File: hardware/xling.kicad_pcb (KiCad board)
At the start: 2 copper layers, 35.6 x 48.3 mm, 58 parts, among them J4 USB_OTG, J5 AVR ISP, J6 Battery, Q1 NTR0202PL, Q2 NTR0202PL, Q3 NTA4153N, SW2 BTN, SW3 BTN, SW4 BTN, U1 LT1109CZ-12, U2 ATMEGA328P-AU, U3 DEP_128064I, U4 MCP73831, U5 AP3401_TSOT26, Y1 8MHz

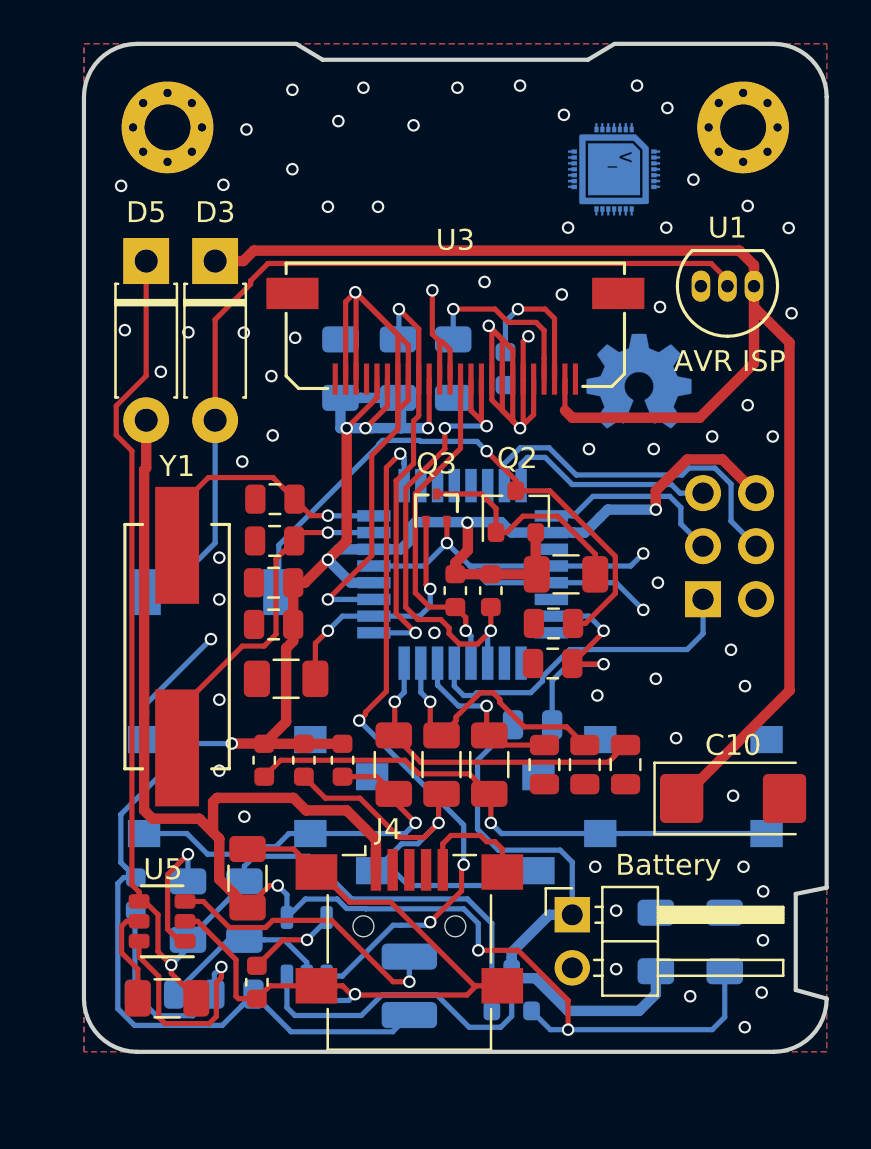
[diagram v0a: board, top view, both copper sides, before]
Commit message: patch 0.2.0004: Updated footprints.
Several footprints were updated to replaced rectangle pads with
rounded-corner pads. Minor PCB changes were made also.

Bill of materials can be found in the hardware directory.

Signed-off-by: Dmitry Salychev <darkness.bsd@gmail.com>
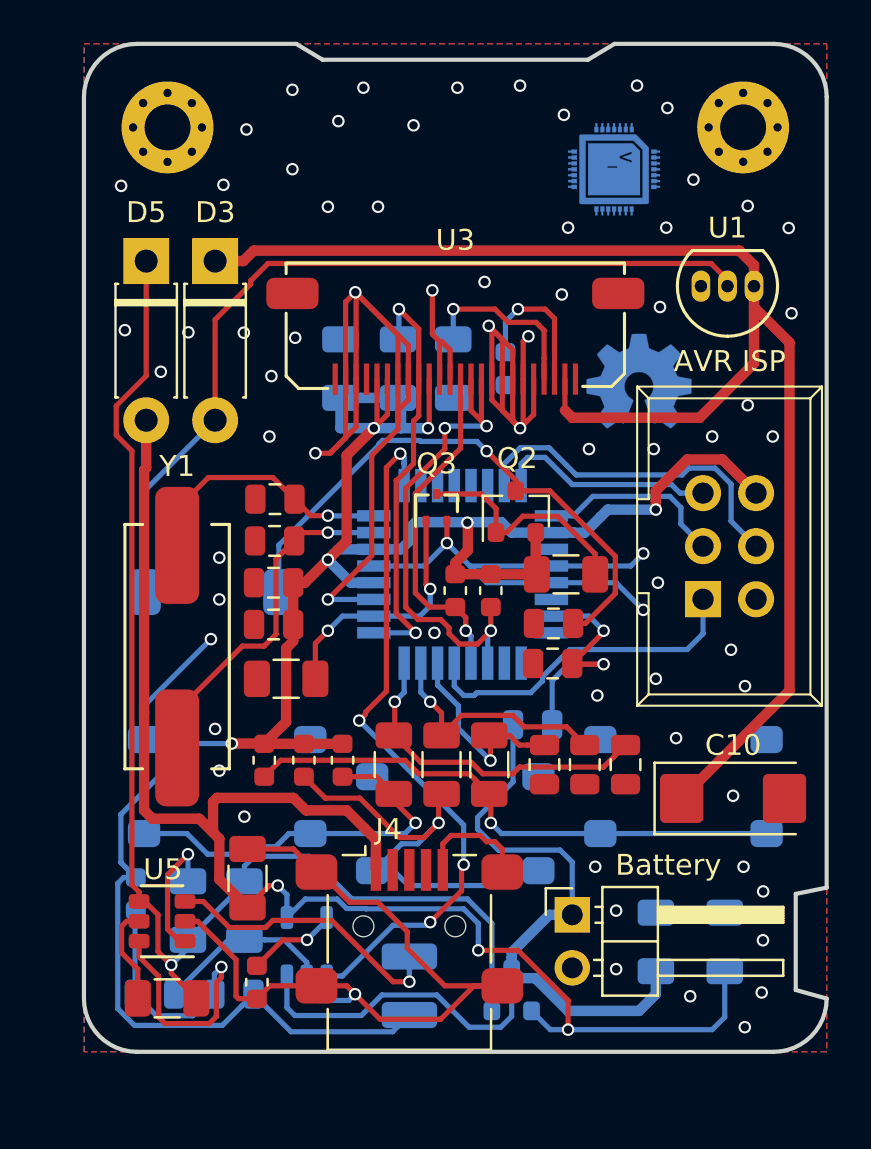
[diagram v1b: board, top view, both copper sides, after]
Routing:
- net GND: track 146.5 -> 157.8 mm
- net /BTN1: track 8.11 -> 10.6 mm
- net /BTN2: track 13.3 -> 12.2 mm
- net Net-(D3-Pad2): track 41.4 -> 40.8 mm
- net +3V3: track 109.3 -> 109.1 mm, vias 7 -> 6
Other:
- board text added: "Xling 0.2.0004 MCUSim.org"
- board text removed: "Xling 0.2.0003 MCUSim.org"

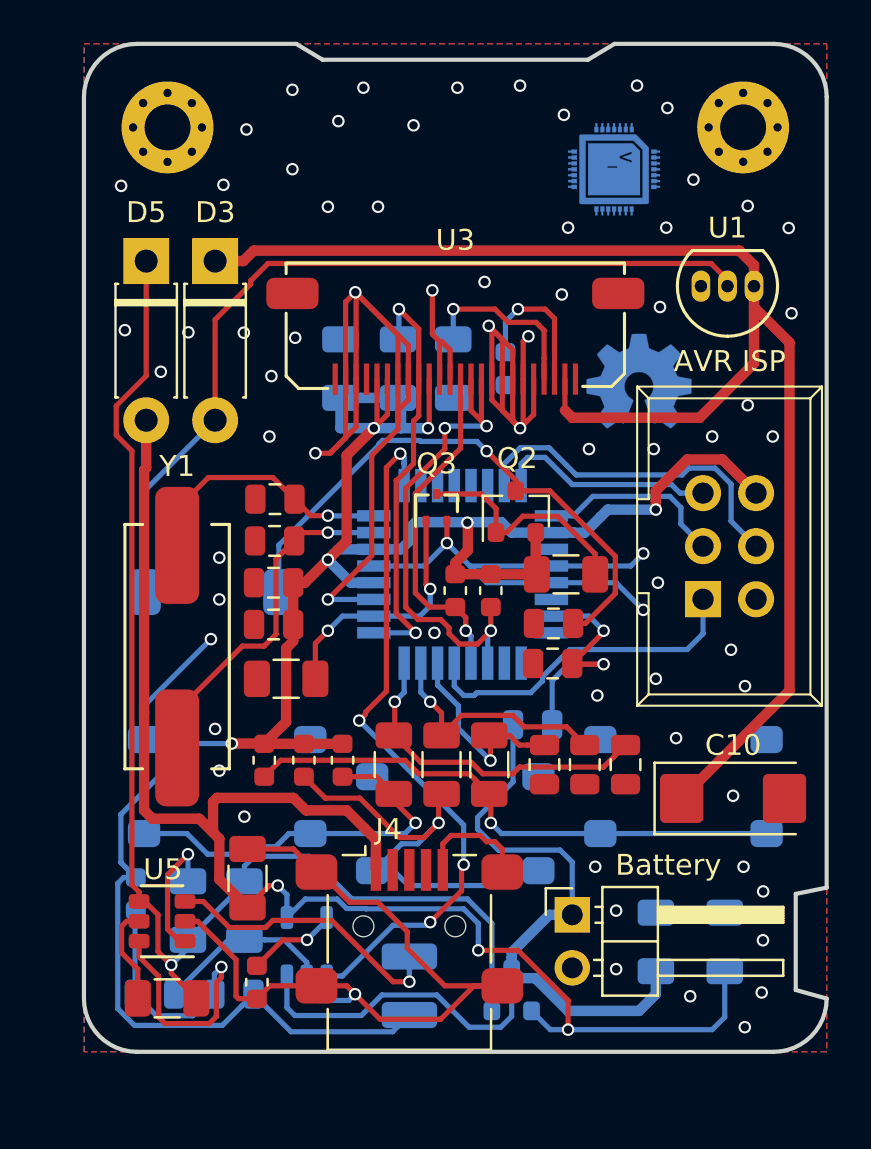
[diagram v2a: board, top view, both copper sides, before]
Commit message: patch 0.2.7: PCB adjustments.
ticket: N/A

There are some modifications to make a new version of the PCB ready for
manufacturing.
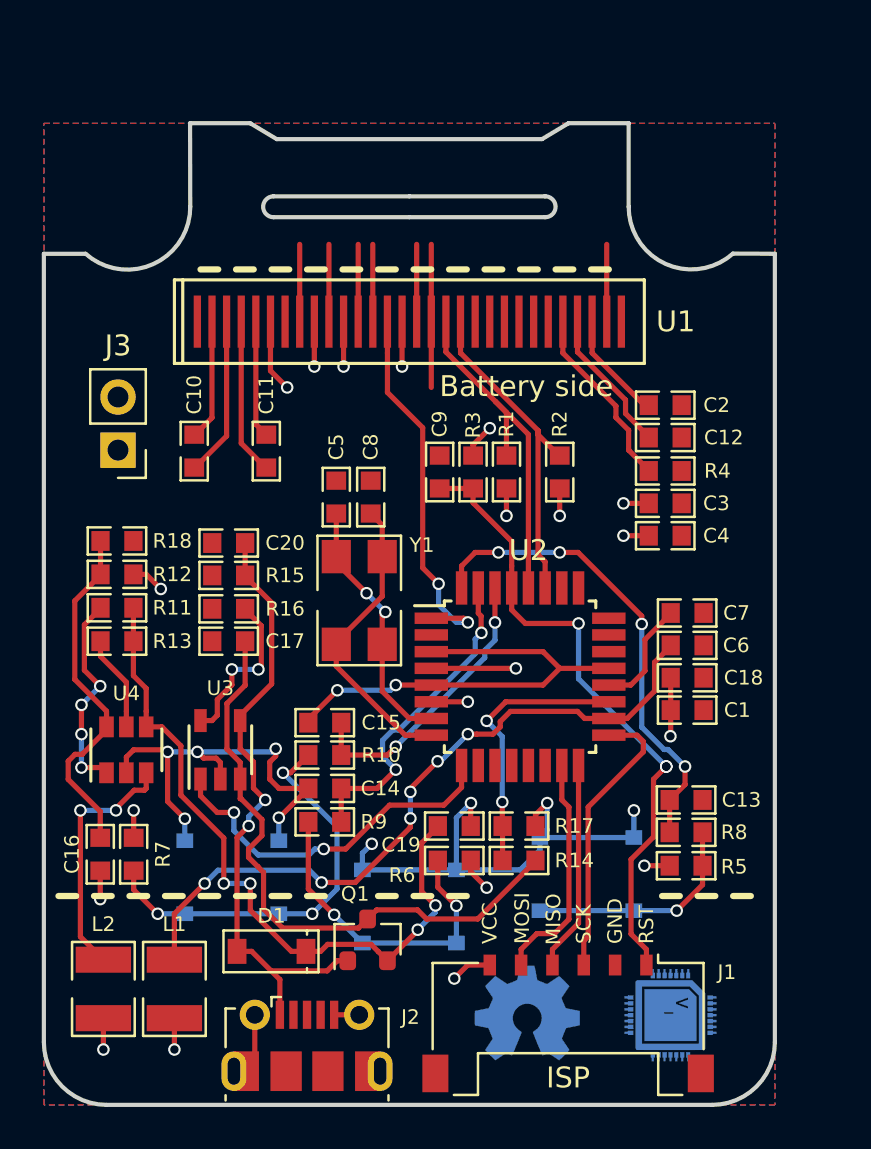
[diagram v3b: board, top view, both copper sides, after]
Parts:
- removed D3, D5: 1N5818, Xling Footprints:D_DO-41_SOD81_P7.62mm_Horizontal
- removed J4: USB_OTG, Xling Footprints:USB_Mini-B_Lumberg_2486_01_Horizontal
- removed J5: AVR ISP, Xling Footprints:IDC-Header_2x03_P2.54mm_Vertical
- removed J6: Battery, Xling Footprints:PinHeader_1x02_P2.54mm_Horizontal
- removed Q2: NTR0202PL, Xling Footprints:SOT-23
- removed Q3: NTA4153N, Xling Footprints:SC-75_SOT-416
- removed R19: 100K, Xling Footprints:R_1206_3216Metric
- removed R20: 110K, Xling Footprints:R_0805_2012Metric
- removed REF** (x2): MountingHole_2.2mm_M2_Pad_Via, MountingHole:MountingHole_2.2mm_M2_Pad_Via
- removed SW4: BTN, Xling Footprints:SW_SPST_PTS645
- removed U5: AP3401_TSOT26, Xling Footprints:AP3401_TSOT26
- added C12: 4.7uF, Xling Footprints:C_0603_1608Metric, F.Cu at (149.8, 95.0)
- added C14: 4.7nF, Xling Footprints:C_0603_1608Metric, F.Cu at (133.4, 111.8)
- added C16: 22pF, Xling Footprints:C_0603_1608Metric, F.Cu at (122.7, 115.0)
- added C17: 4.7uF, Xling Footprints:C_0603_1608Metric, F.Cu at (128.8, 104.8)
- added C4: 4.7uF, Xling Footprints:C_0603_1608Metric, F.Cu at (149.8, 99.8)
- added D1: 1N5819, Xling Footprints:D_SOD-123, F.Cu at (130.9, 119.7)
- added J1: ISP, Xling Footprints:Molex_Pico-Lock_504050-0691_1x06-1MP_P1.50mm_Horizontal, F.Cu at (145.1, 123.1)
- added J2: USB_OTG, Xling Footprints:USB_Micro-B_Molex-105017-0001, F.Cu at (132.6, 124.2)
- added J3: Battery, Xling Footprints:PinHeader_1x02_P2.54mm_Vertical, F.Cu at (123.5, 95.7)
- added SW1: BTN, Xling Footprints:SW_Tact_4.5x4.5mm_TVCM09BB_Low_Profile, B.Cu at (146.0, 116.0)
- C1: value 22pF -> 4.7nF; footprint Xling Footprints:C_0805_2012Metric -> Xling Footprints:C_0603_1608Metric; moved to F.Cu
- C10: value 33uF -> 0.22uF; footprint Xling Footprints:CP_EIA-6032-20_AVX-F -> Xling Footprints:C_0603_1608Metric
- C11: value 2.2uF -> 0.22uF; moved to F.Cu
- C13, C15: value 22pF -> 4.7nF; footprint Xling Footprints:C_0805_2012Metric -> Xling Footprints:C_0603_1608Metric
- C18, C19, C20: value 4.7nF -> 4.7uF; footprint Xling Footprints:C_0805_2012Metric -> Xling Footprints:C_0603_1608Metric
- C2: footprint Xling Footprints:C_1206_3216Metric -> Xling Footprints:C_0603_1608Metric; moved to F.Cu
- C3: footprint Xling Footprints:C_1206_3216Metric -> Xling Footprints:C_0603_1608Metric
- C5: value 4.7uF -> 22pF; footprint Xling Footprints:C_1206_3216Metric -> Xling Footprints:C_0603_1608Metric; moved to F.Cu
- C6: value 4.7uF -> 100nF; footprint Xling Footprints:C_1206_3216Metric -> Xling Footprints:C_0603_1608Metric; moved to F.Cu
- C7: value 4.7nF -> 100nF; footprint Xling Footprints:C_0805_2012Metric -> Xling Footprints:C_0603_1608Metric
- C8: value 100nF -> 22pF; footprint Xling Footprints:C_0805_2012Metric -> Xling Footprints:C_0603_1608Metric
- C9: value 1pF -> 100nF; footprint Xling Footprints:C_0805_2012Metric -> Xling Footprints:C_0603_1608Metric
- L1: value 2.2uH -> 10uH; moved to F.Cu
- L2: value 22uH -> 2.2uH; footprint Xling Footprints:L_7.3x7.3_H3.5 -> Xling Footprints:L_1210_3225Metric; moved to F.Cu
- Q1, R7, U2: moved to F.Cu
- R1: value 100K -> 1K; footprint Xling Footprints:R_1206_3216Metric -> Xling Footprints:R_0603_1608Metric; moved to F.Cu
- R10, R13: footprint Xling Footprints:R_1206_3216Metric -> Xling Footprints:R_0603_1608Metric
- R11: value 191K -> 100K; footprint Xling Footprints:R_0805_2012Metric -> Xling Footprints:R_0603_1608Metric; moved to F.Cu
- R12: value 110K -> 510K; footprint Xling Footprints:R_0805_2012Metric -> Xling Footprints:R_0603_1608Metric
- R14, R15: value 27K -> 510K
- R16: value 27K -> 2.55K
- R17, R18: value 100K -> 110K; footprint Xling Footprints:R_1206_3216Metric -> Xling Footprints:R_0603_1608Metric
- R2: value 910K -> 1K; footprint Xling Footprints:R_1206_3216Metric -> Xling Footprints:R_0603_1608Metric; moved to F.Cu
- R3: value 4K3 -> 10K
- R4, R6: value 100K -> 510K; footprint Xling Footprints:R_1206_3216Metric -> Xling Footprints:R_0603_1608Metric; moved to F.Cu
- R5: value 100K -> 510K; footprint Xling Footprints:R_1206_3216Metric -> Xling Footprints:R_0603_1608Metric
- R8, R9: value 1K -> 100K
- SW2, SW3: footprint Xling Footprints:SW_SPST_PTS645 -> Xling Footprints:SW_Tact_4.5x4.5mm_TVCM09BB_Low_Profile
- U1: value LT1109CZ-12 -> REX012864L; footprint Xling Footprints:TO-92_LT1109CZ -> Xling Footprints:DisplayPin_1x30_P0.7mm
- U3: value DEP_128064I -> MCP73831; footprint Xling Footprints:XF2M_24151AR100_SMD_1x24_Pitch_0.5mm -> Xling Footprints:MCP73831_SOT_23
- U4: value MCP73831 -> AP3401_TSOT26; footprint Xling Footprints:MCP73831_SOT_23 -> Xling Footprints:AP3401_TSOT26; moved to F.Cu
- Y1: value 8MHz -> 12MHz; footprint Xling Footprints:Crystal_HC49-SD_SMD -> Xling Footprints:Crystal_SMD_CFPX-104-4Pin_5x3.2mm
- moved G*** 40.6 mm to (150.0, 122.7)
- moved G*** 30.7 mm to (143.2, 122.7)
- moved C10 30.7 mm to (127.2, 95.7), turned to 270 degrees
- moved C3 26.9 mm to (149.8, 98.2), turned to 0 degrees
- moved U1 26.7 mm to (127.3, 89.5), turned to 0 degrees
- moved R3 26.5 mm to (140.6, 96.7), turned to 90 degrees
- moved C1 25.6 mm to (150.8, 108.1), turned to 0 degrees
- moved U3 23.9 mm to (128.4, 110.0), turned to 0 degrees
- moved C13 23.3 mm to (150.8, 112.4), turned to 0 degrees
- moved R4 22.7 mm to (149.8, 96.7), turned to 180 degrees
- moved C20 21.8 mm to (128.8, 100.1), turned to 180 degrees
- moved R12 21.3 mm to (123.5, 101.6), turned to 0 degrees
- moved R11 20.7 mm to (123.5, 103.2)
- moved C5 20.3 mm to (134.0, 97.9)
- moved C7 19.9 mm to (150.8, 103.5), turned to 0 degrees
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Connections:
- C1 pad 2: Net-(C1-Pad2) -> GND
- C10 pad 1: +12V -> Net-(C10-Pad1)
- C10 pad 2: GND -> Net-(C10-Pad2)
- C11 pad 2: GND -> Net-(C11-Pad2)
- C13 pad 1: Net-(C13-Pad1) -> /BTN3
- C15 pad 1: Net-(C15-Pad1) -> /BTN1
- C18 pad 1: /BTN1 -> +3V3
- C19 pad 1: /BTN2 -> Net-(C19-Pad1)
- C2 pad 1: +3V3 -> Net-(C2-Pad1)
- C20 pad 1: /BTN3 -> Net-(C20-Pad1)
- C3 pad 1: Net-(C3-Pad1) -> +3V3
- C5 pad 1: Net-(C5-Pad1) -> GND
- C5 pad 2: GND -> Net-(C5-Pad2)
- C7 pad 1: +3V3 -> Net-(C7-Pad1)
- C8 pad 1: +3V3 -> GND
- C8 pad 2: GND -> Net-(C8-Pad2)
- C9 pad 1: /OLED_VCC -> /ISP_RST
- L1 pad 1: Net-(L1-Pad1) -> +3V3
- L1 pad 2: +3V3 -> Net-(C6-Pad1)
- L2 pad 1: /OLED_VCC -> Net-(L2-Pad1)
- L2 pad 2: Net-(D3-Pad2) -> +3V3
- Q1 pad 1: Net-(C3-Pad1) -> Net-(C20-Pad1)
- Q1 pad 2: Net-(C5-Pad1) -> Net-(C19-Pad1)
- Q1 pad 3: Net-(C6-Pad1) -> Net-(C17-Pad1)
- R1 pad 2: /OLED_RES -> /OLED_SCL
- R10 pad 1: /OLED_PWR -> /BTN1
- R10 pad 2: GND -> Net-(R10-Pad2)
- R11 pad 1: Net-(C6-Pad1) -> Net-(R11-Pad1)
- R11 pad 2: /BAT_LVL -> Net-(C19-Pad1)
- R12 pad 1: /BAT_LVL -> Net-(C16-Pad2)
- R12 pad 2: GND -> +3V3
- R13 pad 2: Net-(C5-Pad1) -> Net-(C19-Pad1)
- R14 pad 1: +3V3 -> /BAT_LVL
- R14 pad 2: Net-(R14-Pad2) -> Net-(C17-Pad1)
- R15 pad 1: +3V3 -> GND
- R15 pad 2: Net-(R15-Pad2) -> Net-(C20-Pad1)
- R16 pad 1: +3V3 -> Net-(R16-Pad1)
- R16 pad 2: Net-(R16-Pad2) -> GND
- R17 pad 1: /BTN1 -> /BAT_LVL
- R17 pad 2: Net-(R14-Pad2) -> GND
- R18 pad 1: /BTN2 -> GND
- R18 pad 2: Net-(R15-Pad2) -> Net-(C16-Pad2)
- R2 pad 1: GND -> +3V3
- R2 pad 2: Net-(R2-Pad2) -> /OLED_SDA
- R3 pad 1: Net-(R3-Pad1) -> /ISP_RST
- R3 pad 2: GND -> +3V3
- R4 pad 1: Net-(C3-Pad1) -> GND
- R4 pad 2: GND -> Net-(R4-Pad2)
- R5 pad 1: +3V3 -> Net-(R5-Pad1)
- R5 pad 2: Net-(Q2-Pad1) -> +3V3
- R6 pad 2: Net-(C5-Pad1) -> +3V3
- R7 pad 1: Net-(C1-Pad2) -> Net-(R10-Pad2)
- R8 pad 1: +3V3 -> /BTN3
- R8 pad 2: /OLED_SDA -> Net-(R5-Pad1)
- R9 pad 1: +3V3 -> /BTN2
- R9 pad 2: /OLED_SCL -> Net-(R6-Pad1)
- SW2 pad 1: Net-(R14-Pad2) -> Net-(R6-Pad1)
- SW3 pad 1: Net-(R15-Pad2) -> Net-(R10-Pad2)
- U1 pad 1: GND -> (no net)
- U1 pad 2: Net-(D3-Pad2) -> Net-(C10-Pad1)
- U1 pad 3: +12V -> Net-(C10-Pad2)
- U2 pad 18: +3V3 -> Net-(C6-Pad1)
- U2 pad 19: (no net) -> /BAT_LVL
- U2 pad 2: /OLED_PWR -> (no net)
- U2 pad 20: GND -> Net-(C7-Pad1)
- U2 pad 23: /BAT_LVL -> (no net)
- U2 pad 7: Net-(C13-Pad1) -> Net-(C5-Pad2)
- U2 pad 8: Net-(C15-Pad1) -> Net-(C8-Pad2)
- U3 pad 1: (no net) -> /BAT_STAT
- U3 pad 3: GND -> Net-(C17-Pad1)
- U3 pad 4: (no net) -> Net-(C20-Pad1)
- U3 pad 5: +3V3 -> Net-(R16-Pad1)
- U4 pad 1: /BAT_STAT -> Net-(R11-Pad1)
- U4 pad 3: Net-(C6-Pad1) -> Net-(L2-Pad1)
- U4 pad 4: Net-(C3-Pad1) -> Net-(C19-Pad1)
- U4 pad 5: Net-(R3-Pad1) -> Net-(R13-Pad1)
- Y1 pad 1: Net-(C15-Pad1) -> Net-(C8-Pad2)
- Y1 pad 2: Net-(C13-Pad1) -> Net-(C5-Pad2)
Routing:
- net Net-(C3-Pad1): track 72.4 -> 0.00 mm, vias 3 -> 0
- net +3V3: track 109.1 -> 37.3 mm, vias 6 -> 20
- net +12V: track 70.1 -> 0.00 mm
- net Net-(C5-Pad1): track 61.4 -> 0.00 mm, vias 1 -> 0
- net GND: track 157.8 -> 101.2 mm, vias 70 -> 11
- net Net-(D3-Pad2): track 40.8 -> 0.00 mm
- net Net-(C19-Pad1): track 0.00 -> 33.8 mm, vias 0 -> 4
- net Net-(C20-Pad1): track 0.00 -> 30.1 mm, vias 0 -> 2
- net Net-(C17-Pad1): track 0.00 -> 29.6 mm
- net /OLED_VCC: track 27.5 -> 0.00 mm, vias 1 -> 0
- net Net-(R14-Pad2): track 26.6 -> 0.00 mm, vias 1 -> 0
- net Net-(R15-Pad2): track 22.8 -> 0.00 mm, vias 1 -> 0
- net Net-(C1-Pad2): track 20.3 -> 0.00 mm, vias 1 -> 0
- net Net-(R10-Pad2): track 0.00 -> 19.9 mm, vias 0 -> 3
- net Net-(R16-Pad2): track 18.7 -> 0.00 mm, vias 1 -> 0
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- added copper zone on B.Cu, net +3V3
- removed copper zone on B.Cu, net GND
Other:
- board size 35.6 x 48.3 mm -> 35 x 47 mm
- board text added: "0.2.6 3.3V 128x64"
- board text added: "Battery side"
- board text added: "Display side"
- board text added: "GND"
- board text added: "ISP"
- board text added: "MISO"
- board text added: "MOSI"
- board text added: "RST"
- board text added: "Rev: Vcc: Display:"
- board text added: "SCK"
- board text added: "VCC"
- board text removed: "Xling 0.2.0004 MCUSim.org"

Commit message: patch 0.2.8: Add micro USB 3D model.
ticket: N/A
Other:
- board text added: "0.2.8 3.3V 128x64 1.28""
- board text removed: "0.2.6 3.3V 128x64"
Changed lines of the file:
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@@
     (title "Xling PCB")
     (date 2018-11-04)
-    (rev 0.2.7)
+    (rev 0.2.8)
     (company MCUSim)
   )
@@
       (rotate (xyz 0 0 0))
     )
+    (model ${KISYS3DMOD}/Connector_USB.3dshapes/USB_Micro-B_Molex_47346-0001.step
+      (at (xyz 0 0 0))
+      (scale (xyz 1 1 1))
+      (rotate (xyz 0 0 0))
+    )
   )
   (module "Xling Footprints:PinHeader_1x02_P2.54mm_Vertical" (layer F.Cu)
@@
       (effects (font (size 1 1) (thickness 0.15)))
     )
-    (fp_line (start -0.8 0.4) (end -0.8 -0.4) (layer F.Fab) (width 0.1))
-    (fp_line (start -0.8 -0.4) (end 0.8 -0.4) (layer F.Fab) (width 0.1))
-    (fp_line (start 0.8 -0.4) (end 0.8 0.4) (layer F.Fab) (width 0.1))
-    (fp_line (start 0.8 0.4) (end -0.8 0.4) (layer F.Fab) (width 0.1))
-    (fp_line (start -1.4 -0.65) (end -0.3 -0.65) (layer F.SilkS) (width 0.12))
+    (fp_line (start 0.3 0.65) (end 1.4 0.65) (layer F.SilkS) (width 0.12))
+    (fp_line (start -1.4 0.65) (end -0.3 0.65) (layer F.SilkS) (width 0.12))
+    (fp_line (start 0.3 -0.65) (end 1.4 -0.65) (layer F.SilkS) (width 0.12))
+    (fp_line (start 1.4 -0.65) (end 1.4 0.65) (layer F.SilkS) (width 0.12))
+    (fp_line (start -1.4 -0.65) (end -1.4 0.65) (layer F.SilkS) (width 0.12))
+    (fp_text user %R (at 0 0 90) (layer F.Fab)
+      (effects (font (size 0.4 0.4) (thickness 0.06)))
+    )
+    (fp_line (start 1.5 0.75) (end -1.5 0.75) (layer F.CrtYd) (width 0.05))
+    (fp_line (start 1.5 -0.75) (end 1.5 0.75) (layer F.CrtYd) (width 0.05))
+    (fp_line (start -1.5 -0.75) (end 1.5 -0.75) (layer F.CrtYd) (width 0.05))
     (fp_line (start -1.5 0.75) (end -1.5 -0.75) (layer F.CrtYd) (width 0.05))
-    (fp_line (start -1.5 -0.75) (end 1.5 -0.75) (layer F.CrtYd) (width 0.05))
-    (fp_line (start 1.5 -0.75) (end 1.5 0.75) (layer F.CrtYd) (width 0.05))
-    (fp_line (start 1.5 0.75) (end -1.5 0.75) (layer F.CrtYd) (width 0.05))
-    (fp_text user %R (at 0 0 90) (layer F.Fab)
-      (effects (font (size 0.4 0.4) (thickness 0.06)))
-    )
-    (fp_line (start -1.4 -0.65) (end -1.4 0.65) (layer F.SilkS) (width 0.12))
-    (fp_line (start 1.4 -0.65) (end 1.4 0.65) (layer F.SilkS) (width 0.12))
-    (fp_line (start 0.3 -0.65) (end 1.4 -0.65) (layer F.SilkS) (width 0.12))
-    (fp_line (start -1.4 0.65) (end -0.3 0.65) (layer F.SilkS) (width 0.12))
-    (fp_line (start 0.3 0.65) (end 1.4 0.65) (layer F.SilkS) (width 0.12))
+    (fp_line (start -1.4 -0.65) (end -0.3 -0.65) (layer F.SilkS) (width 0.12))
+    (fp_line (start 0.8 0.4) (end -0.8 0.4) (layer F.Fab) (width 0.1))
+    (fp_line (start 0.8 -0.4) (end 0.8 0.4) (layer F.Fab) (width 0.1))
+    (fp_line (start -0.8 -0.4) (end 0.8 -0.4) (layer F.Fab) (width 0.1))
+    (fp_line (start -0.8 0.4) (end -0.8 -0.4) (layer F.Fab) (width 0.1))
+    (pad 2 smd rect (at 0.7875 0 90) (size 0.875 0.95) (layers F.Cu F.Paste F.Mask)
+      (net 12 /OLED_SDA))
     (pad 1 smd rect (at -0.7875 0 90) (size 0.875 0.95) (layers F.Cu F.Paste F.Mask)
       (net 1 +3V3))
-    (pad 2 smd rect (at 0.7875 0 90) (size 0.875 0.95) (layers F.Cu F.Paste F.Mask)
-      (net 12 /OLED_SDA))
     (model ${KISYS3DMOD}/Resistor_SMD.3dshapes/R_0603_1608Metric.wrl
       (at (xyz 0 0 0))
@@
     (effects (font (size 1.5 1.5) (thickness 0.3)) (justify left mirror))
   )
-  (gr_text "0.2.6\n3.3V\n128x64" (at 141 98) (layer B.SilkS)
+  (gr_text "0.2.8\n3.3V\n128x64 1.28\"" (at 141 98) (layer B.SilkS)
     (effects (font (size 1.5 1.5) (thickness 0.3)) (justify left mirror))
   )
